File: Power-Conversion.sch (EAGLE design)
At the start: 70 parts, among them J1 AVR_SPI_PRG_6PTH, U1 ATMEGA328P_TQFP, U2 LM1085IS-3.3

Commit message: After 8 hours of continuous work, I am 90% done with the power distribution board
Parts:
- added C4, C5: 1uF, SparkFun-Capacitors:0.1UF-25V(+80/-20%)(0603)
- added ESC_GND1, ESC_GND10, ESC_GND11, ESC_GND12, ESC_GND2, ESC_GND3, ESC_GND4, ESC_GND5, ESC_GND6, ESC_GND7, ESC_GND8, ESC_GND9: (no value), SparkFun-Connectors:M01PTH
- added U$9: FT230XS, USB-UART:FT230XS
- added U3: LM1085IS-3.3, PowerComponents:LM1085IS-3.3
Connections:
- new net +5_SERVO: C4.1, U2.OUT, U2.VOUT
- net +5V: now also C5.1, U3.OUT, U3.VOUT; no longer U2.OUT, U2.VOUT
- net GND: now also C4.2, C5.2, ESC_GND1.1, ESC_GND10.1, ESC_GND11.1, ESC_GND12.1, ESC_GND2.1, ESC_GND3.1, ESC_GND4.1, ESC_GND5.1, ESC_GND6.1, ESC_GND7.1, ESC_GND8.1, ESC_GND9.1, U$9.GND, U3.ADJ/GND
- net VCC: now also U3.IN
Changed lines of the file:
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@@
 <?xml version="1.0" encoding="utf-8"?>
 <!DOCTYPE eagle SYSTEM "eagle.dtd">
-<eagle version="7.6.0">
+<eagle version="7.7.0">
 <drawing>
 <settings>
@@
 <part name="P+10" library="supply1" deviceset="VCC" device=""/>
 <part name="GND14" library="supply1" deviceset="GND" device=""/>
-<part name="P+12" library="supply1" deviceset="+5V" device=""/>
 <part name="R3" library="SparkFun-Resistors" deviceset="10KOHM-1/10W-1%(0603)" device="0603" value="10K"/>
 <part name="P+14" library="supply1" deviceset="+5V" device=""/>
@@
 <part name="F11" library="PowerComponents" deviceset="PTC(2920L)" device="" value="10A"/>
 <part name="F12" library="PowerComponents" deviceset="PTC(2920L)" device="" value="10A"/>
+<part name="ESC_GND1" library="SparkFun-Connectors" deviceset="M01" device="PTH"/>
+<part name="ESC_GND3" library="SparkFun-Connectors" deviceset="M01" device="PTH"/>
+<part name="ESC_GND5" library="SparkFun-Connectors" deviceset="M01" device="PTH"/>
+<part name="ESC_GND2" library="SparkFun-Connectors" deviceset="M01" device="PTH"/>
+<part name="ESC_GND4" library="SparkFun-Connectors" deviceset="M01" device="PTH"/>
+<part name="ESC_GND6" library="SparkFun-Connectors" deviceset="M01" device="PTH"/>
+<part name="ESC_GND7" library="SparkFun-Connectors" deviceset="M01" device="PTH"/>
+<part name="ESC_GND9" library="SparkFun-Connectors" deviceset="M01" device="PTH"/>
+<part name="ESC_GND8" library="SparkFun-Connectors" deviceset="M01" device="PTH"/>
+<part name="ESC_GND10" library="SparkFun-Connectors" deviceset="M01" device="PTH"/>
+<part name="ESC_GND11" library="SparkFun-Connectors" deviceset="M01" device="PTH"/>
+<part name="ESC_GND12" library="SparkFun-Connectors" deviceset="M01" device="PTH"/>
+<part name="GND21" library="supply1" deviceset="GND" device=""/>
+<part name="GND22" library="supply1" deviceset="GND" device=""/>
+<part name="C4" library="SparkFun-Capacitors" deviceset="0.1UF-25V(+80/-20%)(0603)" device="" value="1uF"/>
+<part name="GND23" library="supply1" deviceset="GND" device=""/>
+<part name="U3" library="PowerComponents" deviceset="LM1085IS-3.3" device=""/>
+<part name="P+8" library="supply1" deviceset="VCC" device=""/>
+<part name="GND24" library="supply1" deviceset="GND" device=""/>
+<part name="P+9" library="supply1" deviceset="+5V" device=""/>
+<part name="C5" library="SparkFun-Capacitors" deviceset="0.1UF-25V(+80/-20%)(0603)" device="" value="1uF"/>
+<part name="GND25" library="supply1" deviceset="GND" device=""/>
+<part name="U$9" library="USB-UART" deviceset="FT230XS" device=""/>
+<part name="GND26" library="supply1" deviceset="GND" device=""/>
 </parts>
 <sheets>
@@
 <instance part="P+10" gate="VCC" x="203.2" y="127"/>
 <instance part="GND14" gate="1" x="203.2" y="116.84"/>
-<instance part="P+12" gate="1" x="251.46" y="124.46"/>
 <instance part="R3" gate="G$1" x="271.78" y="116.84"/>
 <instance part="P+14" gate="1" x="266.7" y="127"/>
@@
 <instance part="F11" gate="G$1" x="170.18" y="-25.4" rot="R180"/>
 <instance part="F12" gate="G$1" x="170.18" y="-40.64" rot="R180"/>
+<instance part="ESC_GND1" gate="G$1" x="388.62" y="25.4" rot="MR180"/>
+<instance part="ESC_GND3" gate="G$1" x="388.62" y="12.7" rot="MR180"/>
+<instance part="ESC_GND5" gate="G$1" x="388.62" y="0" rot="MR180"/>
+<instance part="ESC_GND2" gate="G$1" x="414.02" y="25.4" rot="MR0"/>
+<instance part="ESC_GND4" gate="G$1" x="414.02" y="12.7" rot="MR0"/>
+<instance part="ESC_GND6" gate="G$1" x="414.02" y="0" rot="MR0"/>
+<instance part="ESC_GND7" gate="G$1" x="429.26" y="25.4" rot="MR180"/>
+<instance part="ESC_GND9" gate="G$1" x="429.26" y="12.7" rot="MR180"/>
+<instance part="ESC_GND8" gate="G$1" x="457.2" y="25.4" rot="MR0"/>
+<instance part="ESC_GND10" gate="G$1" x="457.2" y="12.7" rot="MR0"/>
+<instance part="ESC_GND11" gate="G$1" x="429.26" y="0" rot="MR180"/>
+<instance part="ESC_GND12" gate="G$1" x="457.2" y="0" rot="MR0"/>
+<instance part="GND21" gate="1" x="401.32" y="-7.62" rot="MR0"/>
+<instance part="GND22" gate="1" x="441.96" y="-7.62" rot="MR0"/>
+<instance part="C4" gate="G$1" x="243.84" y="114.3"/>
+<instance part="GND23" gate="1" x="243.84" y="106.68"/>
+<instance part="U3" gate="A" x="226.06" y="157.48"/>
+<instance part="P+8" gate="VCC" x="205.74" y="160.02"/>
+<instance part="GND24" gate="1" x="205.74" y="149.86"/>
+<instance part="P+9" gate="1" x="254" y="157.48"/>
+<instance part="C5" gate="G$1" x="246.38" y="147.32"/>
+<instance part="GND25" gate="1" x="246.38" y="139.7"/>
+<instance part="U$9" gate="G$1" x="83.82" y="198.12" rot="MR0"/>
+<instance part="GND26" gate="1" x="83.82" y="175.26"/>
 </instances>
 <busses>
@@
 <junction x="160.02" y="81.28"/>
 </segment>
+<segment>
+<pinref part="U3" gate="A" pin="IN"/>
+<pinref part="P+8" gate="VCC" pin="VCC"/>
+</segment>
 </net>
 <net name="GND" class="0">
@@
 <wire x1="180.34" y1="-45.72" x2="182.88" y2="-45.72" width="0.1524" layer="91"/>
 </segment>
+<segment>
+<pinref part="ESC_GND1" gate="G$1" pin="1"/>
+<pinref part="ESC_GND2" gate="G$1" pin="1"/>
+<wire x1="396.24" y1="25.4" x2="401.32" y2="25.4" width="0.1524" layer="91"/>
+<pinref part="ESC_GND3" gate="G$1" pin="1"/>
+<pinref part="ESC_GND4" gate="G$1" pin="1"/>
+<wire x1="401.32" y1="25.4" x2="406.4" y2="25.4" width="0.1524" layer="91"/>
+<wire x1="396.24" y1="12.7" x2="401.32" y2="12.7" width="0.1524" layer="91"/>
+<wire x1="401.32" y1="12.7" x2="406.4" y2="12.7" width="0.1524" layer="91"/>
+<wire x1="401.32" y1="25.4" x2="401.32" y2="12.7" width="0.1524" layer="91"/>
+<junction x="401.32" y="25.4"/>
+<junction x="401.32" y="12.7"/>
+<pinref part="ESC_GND5" gate="G$1" pin="1"/>
+<pinref part="ESC_GND6" gate="G$1" pin="1"/>
+<wire x1="396.24" y1="0" x2="401.32" y2="0" width="0.1524" layer="91"/>
+<wire x1="401.32" y1="0" x2="406.4" y2="0" width="0.1524" layer="91"/>
+<wire x1="401.32" y1="12.7" x2="401.32" y2="0" width="0.1524" layer="91"/>
+<junction x="401.32" y="0"/>
+<pinref part="GND21" gate="1" pin="GND"/>
+<wire x1="401.32" y1="0" x2="401.32" y2="-5.08" width="0.1524" layer="91"/>
+</segment>
+<segment>
+<pinref part="ESC_GND7" gate="G$1" pin="1"/>
+<pinref part="ESC_GND8" gate="G$1" pin="1"/>
+<wire x1="436.88" y1="25.4" x2="441.96" y2="25.4" width="0.1524" layer="91"/>
+<pinref part="ESC_GND9" gate="G$1" pin="1"/>
+<pinref part="ESC_GND10" gate="G$1" pin="1"/>
+<wire x1="441.96" y1="25.4" x2="449.58" y2="25.4" width="0.1524" layer="91"/>
+<wire x1="436.88" y1="12.7" x2="441.96" y2="12.7" width="0.1524" layer="91"/>
+<wire x1="441.96" y1="12.7" x2="449.58" y2="12.7" width="0.1524" layer="91"/>
+<wire x1="441.96" y1="25.4" x2="441.96" y2="12.7" width="0.1524" layer="91"/>
+<junction x="441.96" y="25.4"/>
+<junction x="441.96" y="12.7"/>
+<wire x1="441.96" y1="12.7" x2="441.96" y2="0" width="0.1524" layer="91"/>
+<pinref part="ESC_GND11" gate="G$1" pin="1"/>
+<wire x1="441.96" y1="0" x2="436.88" y2="0" width="0.1524" layer="91"/>
+<pinref part="ESC_GND12" gate="G$1" pin="1"/>
+<wire x1="441.96" y1="0" x2="449.58" y2="0" width="0.1524" layer="91"/>
+<junction x="441.96" y="0"/>
+<pinref part="GND22" gate="1" pin="GND"/>
+<wire x1="441.96" y1="0" x2="441.96" y2="-5.08" width="0.1524" layer="91"/>
+</segment>
+<segment>
+<pinref part="C4" gate="G$1" pin="2"/>
+<pinref part="GND23" gate="1" pin="GND"/>
+<wire x1="243.84" y1="111.76" x2="243.84" y2="109.22" width="0.1524" layer="91"/>
+</segment>
+<segment>
+<pinref part="U3" gate="A" pin="ADJ/GND"/>
+<pinref part="GND24" gate="1" pin="GND"/>
+</segment>
+<segment>
+<pinref part="C5" gate="G$1" pin="2"/>
+<pinref part="GND25" gate="1" pin="GND"/>
+<wire x1="246.38" y1="144.78" x2="246.38" y2="142.24" width="0.1524" layer="91"/>
+</segment>
+<segment>
+<pinref part="GND26" gate="1" pin="GND"/>
+<pinref part="U$9" gate="G$1" pin="GND"/>
+<wire x1="83.82" y1="177.8" x2="83.82" y2="180.34" width="0.1524" layer="91"/>
+</segment>
 </net>
 <net name="SCL" class="0">
@@
 </net>
 <net name="+5V" class="0">
-<segment>
-<pinref part="U2" gate="A" pin="OUT"/>
-<pinref part="U2" gate="A" pin="VOUT"/>
-<wire x1="243.84" y1="124.46" x2="243.84" y2="121.92" width="0.1524" layer="91"/>
-<wire x1="243.84" y1="121.92" x2="251.46" y2="121.92" width="0.1524" layer="91"/>
-<junction x="243.84" y="121.92"/>
-<pinref part="P+12" gate="1" pin="+5V"/>
-</segment>
 <segment>
 <pinref part="U1" gate="U$1" pin="VCC@4"/>
@@
 <junction x="469.9" y="109.22"/>
 </segment>
+<segment>
+<pinref part="U3" gate="A" pin="OUT"/>
+<pinref part="U3" gate="A" pin="VOUT"/>
+<wire x1="246.38" y1="157.48" x2="246.38" y2="154.94" width="0.1524" layer="91"/>
+<wire x1="246.38" y1="154.94" x2="254" y2="154.94" width="0.1524" layer="91"/>
+<junction x="246.38" y="154.94"/>
+<pinref part="P+9" gate="1" pin="+5V"/>
+<pinref part="C5" gate="G$1" pin="1"/>
+<wire x1="246.38" y1="154.94" x2="246.38" y2="152.4" width="0.1524" layer="91"/>
+</segment>
 </net>
 <net name="N$13" class="0">
@@
 </segment>
 </net>
+<net name="+5_SERVO" class="0">
+<segment>
+<pinref part="U2" gate="A" pin="OUT"/>
+<pinref part="U2" gate="A" pin="VOUT"/>
+<wire x1="243.84" y1="124.46" x2="243.84" y2="121.92" width="0.1524" layer="91"/>
+<wire x1="243.84" y1="121.92" x2="251.46" y2="121.92" width="0.1524" layer="91"/>
+<junction x="243.84" y="121.92"/>
+<pinref part="C4" gate="G$1" pin="1"/>
+<wire x1="243.84" y1="121.92" x2="243.84" y2="119.38" width="0.1524" layer="91"/>
+<label x="246.38" y="121.92" size="1.778" layer="95"/>
+</segment>
+</net>

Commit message: Finished most of the wiring.  Also changed pwm chips and FTDI chips
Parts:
- removed C3: 0.1uF, SparkFun-Capacitors:0.1UF-25V(+80/-20%)(0603)
- removed R6: 470, SparkFun-Resistors:470OHM1/10W1%(0603)
- removed U$8: TLC59401PWPR, MotherboardParts:TLC59401PWPR
- removed U$9: FT230XS, USB-UART:FT230XS
- added C6: 10uF, SparkFun-Capacitors:0.1UF-25V(+80/-20%)(0603)
- added CAMDATA, CAMDATA1: T2I, BACKPLANE:T2I
- added LED1: Red, SparkFun:LED0603
- added LED2: Green, SparkFun:LED0603
- added R7: 10k, SparkFun-Resistors:470OHM1/10W1%(0603)
- added SJ_A0, SJ_A1: (no value), microbuilder:SOLDERJUMPERREFLOW_NOPASTE
- added U4: PCA9685, microbuilder:PCA9685
- added U5: FT232RLSSOP, SparkFun:FT232RLSSOP
- R4: device SparkFun-Resistors:1KOHM-1/10W-1%(0603) -> SparkFun:RESISTOR0402-RES
- R5: value 470 -> 1K; device SparkFun-Resistors:470OHM1/10W1%(0603) -> SparkFun:RESISTOR0402-RES
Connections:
- removed net N$25: R4.2, U$8.IREF
- new net CTS: U1.PC3(ADC3), U5.CTS
- new net DTR: U1.PD2(INT0), U5.DTR
- new net N$35: R7.2, U4.#OE
- new net RXI: U1.PD1(TXD), U5.RXD
- new net RXLED: LED2.C, U5.RXLED
- new net SCL1: SJ_A1.2, U$1.SCL, U$2.SCL, U$3.SCL
- new net SDA1: SJ_A0.2, U$1.SDA, U$2.SDA, U$3.SDA
- new net TXLED: LED1.C, U5.TXLED
- new net TXO: U1.PD0(RXD), U5.TXD
- new net USB_D+: CAMDATA1.1, U5.USBDP
- new net USB_D-: CAMDATA1.2, U5.USBDM
- net +5V: now also C6.1, R4.2, R5.2, U4.VDD, U5.VCC, U5.VCCIO; no longer C3.1, U$8.TEST, U$8.VCC
- net GND: now also C6.2, CAMDATA.2, CAMDATA.3, CAMDATA.4, R7.1, U4.A0, U4.A1, U4.A2, U4.A3, U4.A4, U4.A5, U4.EXTCLK, U4.GND, U5.AGND, U5.GND18, U5.GND21, U5.GND7, U5.TEST; no longer C3.2, R4.1, U$8.GND, U$8.MODE, U$9.GND
- net GSCLK: no longer U$8.GSCLK
- net N$12: now also LED1.A, R4.1; no longer R5.1, U$8.SCLK
- net N$13: no longer U$8.XLAT
- net N$14: now also LED2.A, R5.1; no longer R6.1, U$8.SIN
- net N$15: now also U4.PWM0; no longer U$8.OUT0
- net N$16: now also U4.PWM1; no longer U$8.OUT1
- net N$17: now also U4.PWM2; no longer U$8.OUT2
- net N$18: now also U4.PWM3; no longer U$8.OUT3
- net N$19: now also U4.PWM4; no longer U$8.OUT4
- net N$2: now also U4.PWM10; no longer U$8.OUT10
- net N$20: now also U4.PWM5; no longer U$8.OUT5
- net N$21: now also U4.PWM6; no longer U$8.OUT6
- net N$22: now also U4.PWM7; no longer U$8.OUT7
- net N$23: now also U4.PWM8; no longer U$8.OUT8
- net N$24: now also U4.PWM9; no longer U$8.OUT9
- net N$26: no longer R6.2
- net N$27: no longer U$8.BLANK
- net N$31: no longer R5.2
- net N$4: now also U4.PWM11; no longer U$8.OUT11
- net SCL: now also SJ_A1.1, U4.SCL; no longer U$1.SCL, U$2.SCL, U$3.SCL
- net SDA: now also SJ_A0.1, U4.SDA; no longer U$1.SDA, U$2.SDA, U$3.SDA
- net VCC: now also CAMDATA.1, CAMDATA1.3, CAMDATA1.4
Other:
- moved on the sheet: PWM_ESC1, PWM_ESC10, PWM_ESC11, PWM_ESC12, PWM_ESC2, PWM_ESC3, PWM_ESC4, PWM_ESC5, PWM_ESC6, PWM_ESC7, PWM_ESC8, PWM_ESC9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

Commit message: More changes to the board layout.  Should be complete.
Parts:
- removed J1: AVR_SPI_PRG_6PTH, SparkFun-Connectors:AVR_SPI_PRG_6PTH
- added CAMDATA2: T2I, BACKPLANE:T2I
- added D6: (no value), DiscreteComponents:DIODE-DO-214AC
- added SV1, SV2: (no value), con-lstb:MA03-1
- added T3: FDN340P, DiscreteComponents:FDN340P
- added U$8: 8_PIN_HEADER, PowerComponents:8_PIN_HEADER
- V+_ESC1, V+_ESC10, V+_ESC11, V+_ESC12, V+_ESC2, V+_ESC3, V+_ESC4, V+_ESC5, V+_ESC6, V+_ESC7, V+_ESC8, V+_ESC9, V-_ESC1, V-_ESC10, V-_ESC11, V-_ESC12, V-_ESC2, V-_ESC3, V-_ESC4, V-_ESC5, V-_ESC6, V-_ESC7, V-_ESC8, V-_ESC9: value (none) -> 16_GUAGE_WIRE; device SparkFun-Connectors:BANANA_CONN -> PowerComponents:16_GUAGE_WIRE
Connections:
- new net +5V_LIN: C5.1, D6.A, T3.G, U3.OUT, U3.VOUT
- new net +5V_USB: T3.D, U$8.P$8
- new net PWM13: SV1.2, SV2.2, U4.PWM12
- net +5V: now also D6.C, T3.S; no longer C5.1, J1.2, U3.OUT, U3.VOUT
- net +5_SERVO: now also SV1.1, SV2.1
- net GND: now also SV1.3, SV2.3, U$8.P$6, V-_ESC1.P$1, V-_ESC10.P$1, V-_ESC11.P$1, V-_ESC12.P$1, V-_ESC2.P$1, V-_ESC3.P$1, V-_ESC4.P$1, V-_ESC5.P$1, V-_ESC6.P$1, V-_ESC7.P$1, V-_ESC8.P$1, V-_ESC9.P$1; no longer J1.6, V-_ESC1.1, V-_ESC10.1, V-_ESC11.1, V-_ESC12.1, V-_ESC2.1, V-_ESC3.1, V-_ESC4.1, V-_ESC5.1, V-_ESC6.1, V-_ESC7.1, V-_ESC8.1, V-_ESC9.1
- net N$1: now also V+_ESC1.P$1; no longer V+_ESC1.1
- net N$11: now also V+_ESC8.P$1; no longer V+_ESC8.1
- net N$13: now also U$8.P$3; no longer J1.5
- net N$26: now also U$8.P$7; no longer J1.4
- net N$28: now also V+_ESC9.P$1; no longer V+_ESC9.1
- net N$29: now also U$8.P$1; no longer J1.1
- net N$3: now also V+_ESC2.P$1; no longer V+_ESC2.1
- net N$30: now also V+_ESC10.P$1; no longer V+_ESC10.1
- net N$31: now also U$8.P$2; no longer J1.3
- net N$32: now also V+_ESC4.P$1; no longer V+_ESC4.1
- net N$33: now also V+_ESC11.P$1; no longer V+_ESC11.1
- net N$34: now also V+_ESC12.P$1; no longer V+_ESC12.1
- net N$5: now also V+_ESC3.P$1; no longer V+_ESC3.1
- net N$6: now also V+_ESC5.P$1; no longer V+_ESC5.1
- net N$7: now also V+_ESC6.P$1; no longer V+_ESC6.1
- net N$8: now also V+_ESC7.P$1; no longer V+_ESC7.1
- net SCL: now also CAMDATA2.2
- net SDA: now also CAMDATA2.1
- net VCC: now also CAMDATA2.3, CAMDATA2.4
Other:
- moved on the sheet: C6, F1, F10, F11, F12, F2, F3, F4, F5, F6, F7, F8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

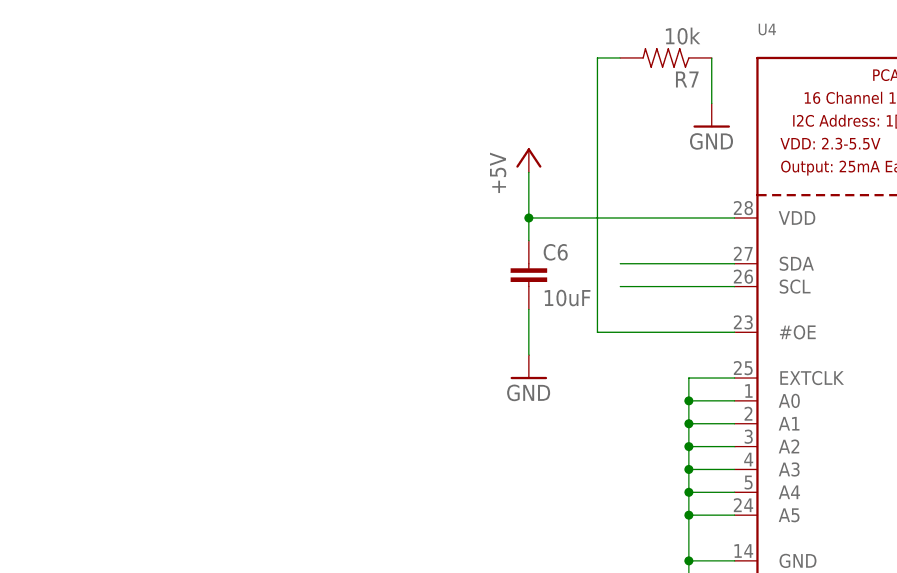
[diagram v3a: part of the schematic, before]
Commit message: Added pull up resistors to I2C lines
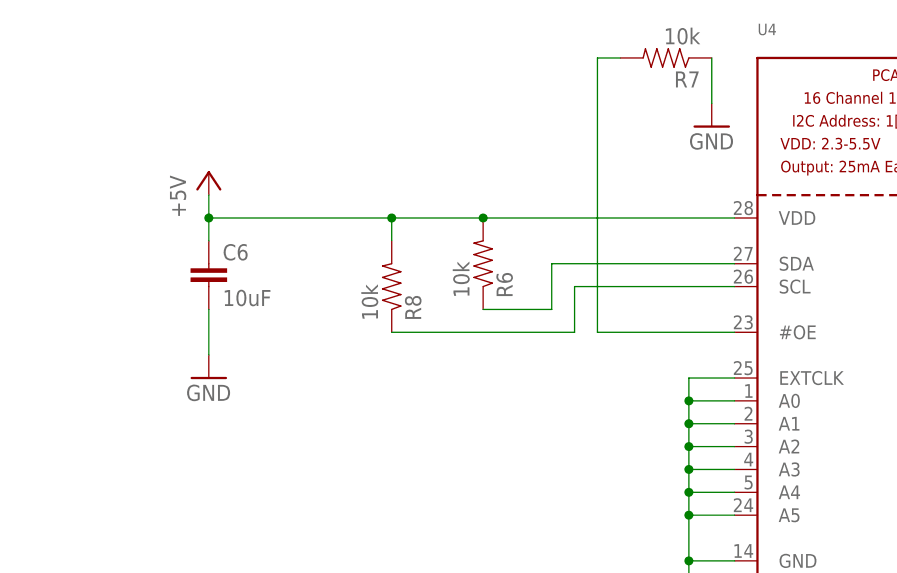
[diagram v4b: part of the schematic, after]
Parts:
- added R6, R8: 10k, SparkFun-Resistors:470OHM1/10W1%(0603)
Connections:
- net +5V: now also R6.2, R8.2
- net SCL: now also R8.1
- net SDA: now also R6.1
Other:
- moved on the sheet: C6
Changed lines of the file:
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@@
 <part name="D6" library="DiscreteComponents" deviceset="DIODE-" device="DO-214AC"/>
 <part name="P+17" library="supply1" deviceset="+5V" device=""/>
+<part name="R6" library="SparkFun-Resistors" deviceset="470OHM1/10W1%(0603)" device="" value="10k"/>
+<part name="R8" library="SparkFun-Resistors" deviceset="470OHM1/10W1%(0603)" device="" value="10k"/>
 </parts>
 <sheets>
@@
 <instance part="GND25" gate="1" x="246.38" y="139.7"/>
 <instance part="U4" gate="G$1" x="391.16" y="208.28"/>
-<instance part="C6" gate="G$1" x="347.98" y="215.9"/>
-<instance part="P+11" gate="1" x="347.98" y="231.14"/>
-<instance part="GND27" gate="1" x="347.98" y="205.74"/>
+<instance part="C6" gate="G$1" x="312.42" y="215.9"/>
+<instance part="P+11" gate="1" x="312.42" y="228.6"/>
+<instance part="GND27" gate="1" x="312.42" y="205.74"/>
 <instance part="R7" gate="G$1" x="363.22" y="241.3" rot="R180"/>
 <instance part="GND28" gate="1" x="368.3" y="233.68"/>
@@
 <instance part="D6" gate="G$1" x="416.56" y="142.24" rot="R270"/>
 <instance part="P+17" gate="1" x="426.72" y="144.78"/>
+<instance part="R6" gate="G$1" x="342.9" y="218.44" rot="MR90"/>
+<instance part="R8" gate="G$1" x="332.74" y="215.9" rot="MR90"/>
 </instances>
 <busses>
@@
 <pinref part="C6" gate="G$1" pin="2"/>
 <pinref part="GND27" gate="1" pin="GND"/>
-<wire x1="347.98" y1="213.36" x2="347.98" y2="208.28" width="0.1524" layer="91"/>
+<wire x1="312.42" y1="213.36" x2="312.42" y2="208.28" width="0.1524" layer="91"/>
 </segment>
 <segment>
@@
 <segment>
 <pinref part="U4" gate="G$1" pin="SCL"/>
-<wire x1="370.84" y1="215.9" x2="358.14" y2="215.9" width="0.1524" layer="91"/>
+<wire x1="370.84" y1="215.9" x2="353.06" y2="215.9" width="0.1524" layer="91"/>
+<pinref part="R8" gate="G$1" pin="1"/>
+<wire x1="332.74" y1="210.82" x2="353.06" y2="210.82" width="0.1524" layer="91"/>
+<wire x1="353.06" y1="210.82" x2="353.06" y2="215.9" width="0.1524" layer="91"/>
 </segment>
 <segment>
@@
 <segment>
 <pinref part="U4" gate="G$1" pin="SDA"/>
-<wire x1="370.84" y1="218.44" x2="358.14" y2="218.44" width="0.1524" layer="91"/>
+<wire x1="370.84" y1="218.44" x2="350.52" y2="218.44" width="0.1524" layer="91"/>
+<pinref part="R6" gate="G$1" pin="1"/>
+<wire x1="342.9" y1="213.36" x2="350.52" y2="213.36" width="0.1524" layer="91"/>
+<wire x1="350.52" y1="213.36" x2="350.52" y2="218.44" width="0.1524" layer="91"/>
 </segment>
 <segment>
@@
 <pinref part="U4" gate="G$1" pin="VDD"/>
 <pinref part="C6" gate="G$1" pin="1"/>
-<wire x1="370.84" y1="223.52" x2="347.98" y2="223.52" width="0.1524" layer="91"/>
-<wire x1="347.98" y1="223.52" x2="347.98" y2="220.98" width="0.1524" layer="91"/>
+<wire x1="370.84" y1="223.52" x2="342.9" y2="223.52" width="0.1524" layer="91"/>
+<wire x1="342.9" y1="223.52" x2="332.74" y2="223.52" width="0.1524" layer="91"/>
+<wire x1="332.74" y1="223.52" x2="312.42" y2="223.52" width="0.1524" layer="91"/>
+<wire x1="312.42" y1="223.52" x2="312.42" y2="220.98" width="0.1524" layer="91"/>
 <pinref part="P+11" gate="1" pin="+5V"/>
-<wire x1="347.98" y1="223.52" x2="347.98" y2="228.6" width="0.1524" layer="91"/>
-<junction x="347.98" y="223.52"/>
-</segment>
-<segment>
+<wire x1="312.42" y1="223.52" x2="312.42" y2="226.06" width="0.1524" layer="91"/>
+<junction x="312.42" y="223.52"/>
+<pinref part="R6" gate="G$1" pin="2"/>
+<junction x="342.9" y="223.52"/>
+<pinref part="R8" gate="G$1" pin="2"/>
+<wire x1="332.74" y1="220.98" x2="332.74" y2="223.52" width="0.1524" layer="91"/>
+<junction x="332.74" y="223.52"/>
+</segment>
+<segment>
